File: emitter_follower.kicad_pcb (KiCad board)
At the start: 2 copper layers, 10 parts, among them Q2201 DNLS350E, Q2202 DPLS350E, Q2203 TIP41C, Q2204 TIP42C

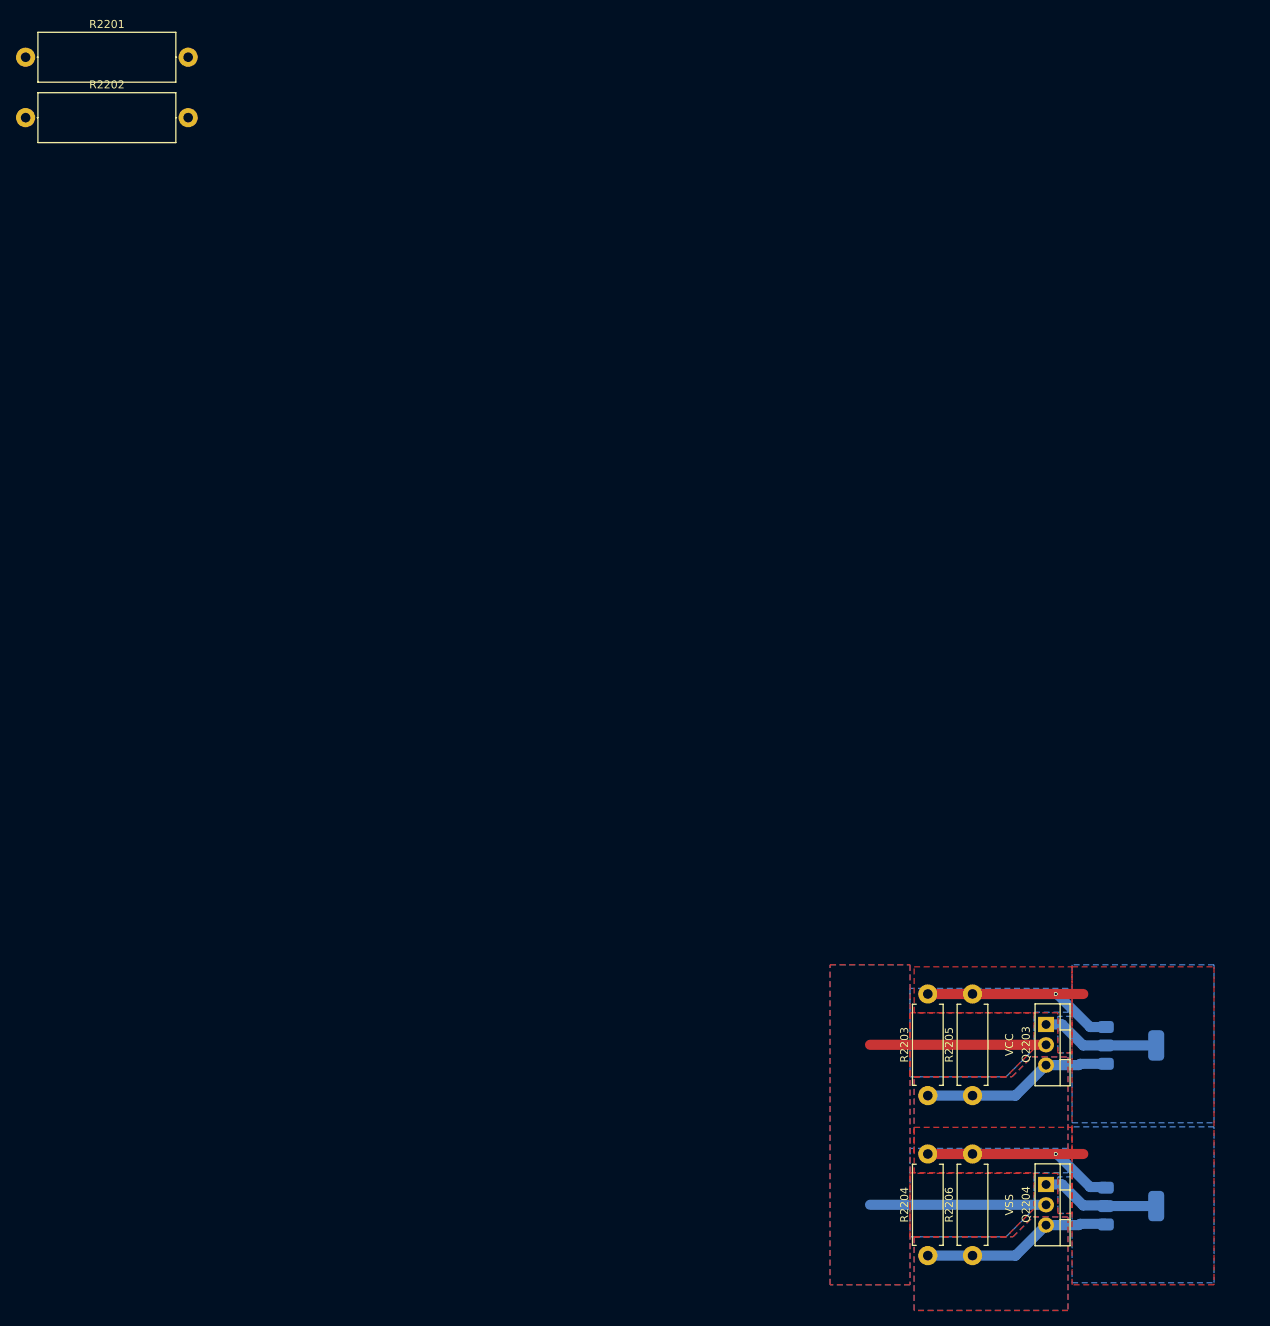
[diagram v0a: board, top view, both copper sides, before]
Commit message: add pcb outstage-unit sub circuit layout of power-electronics
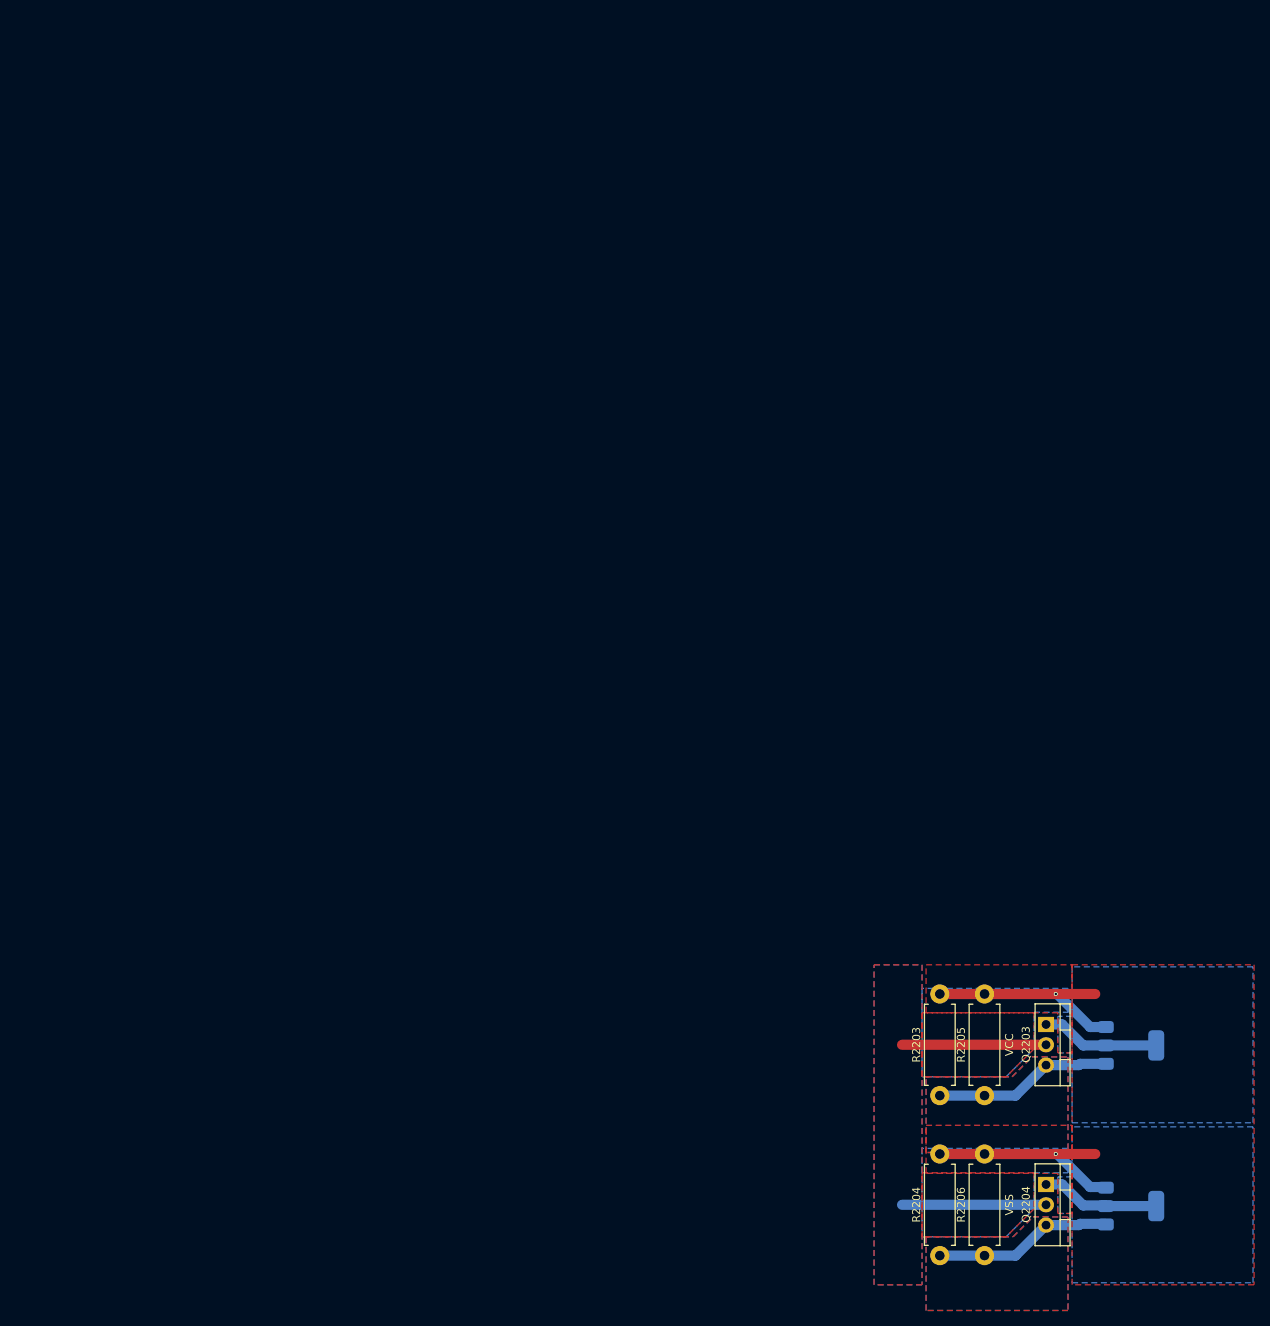
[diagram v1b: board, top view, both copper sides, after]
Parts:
- removed R2201, R2202: 22, pss:R_Axial_DIN0617_L17.0mm_D6.0mm_P20.32mm_Horizontal
- moved R2203 1.50 mm to (83.7, 116.3)
- moved R2204 1.50 mm to (83.7, 123.7)
- moved R2205 1.50 mm to (89.3, 116.3)
- moved R2206 1.50 mm to (89.3, 123.7)
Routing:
- net /VSS: track 22.0 -> 18.0 mm
- net /VCC: track 22.0 -> 18.0 mm
- net /v_out: track 86.8 -> 83.8 mm
- net /2: track 23.9 -> 22.4 mm
- net /1: track 23.9 -> 22.4 mm

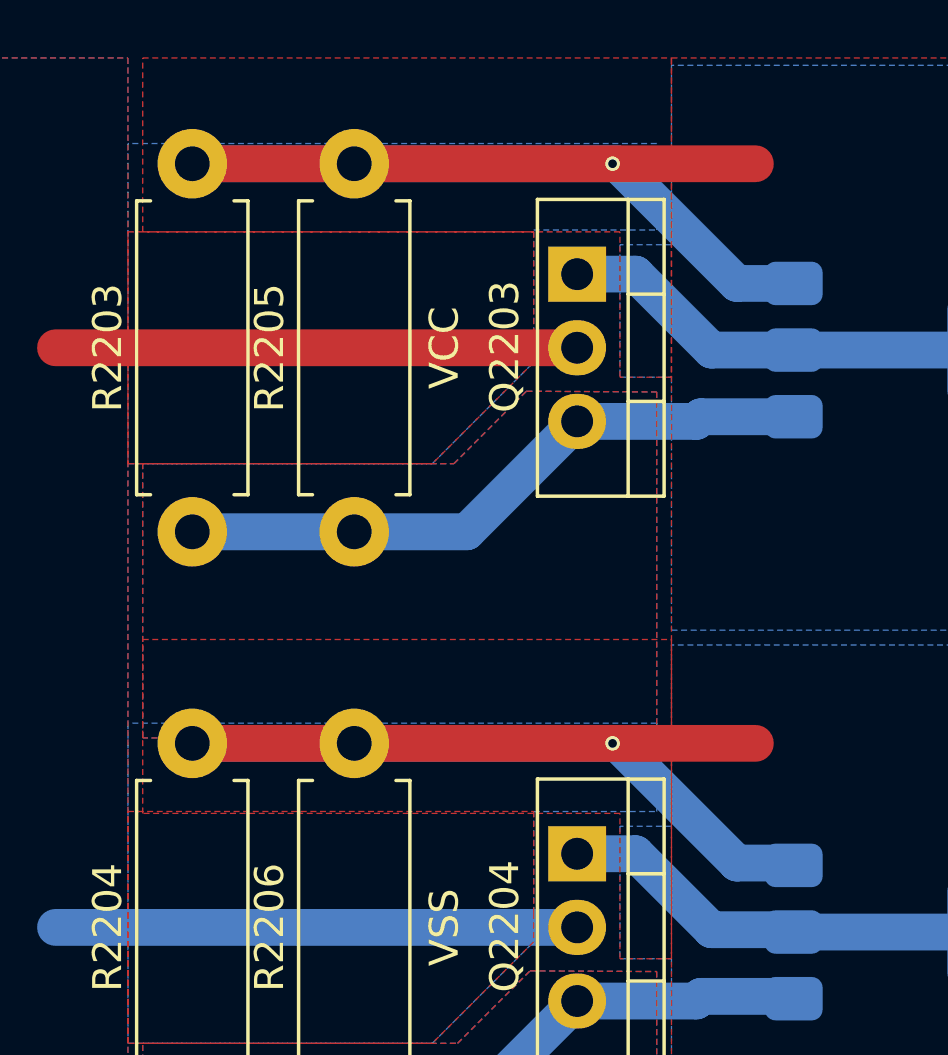
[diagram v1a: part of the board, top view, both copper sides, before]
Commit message: edit heatsink mounting holes position, fix copper pour
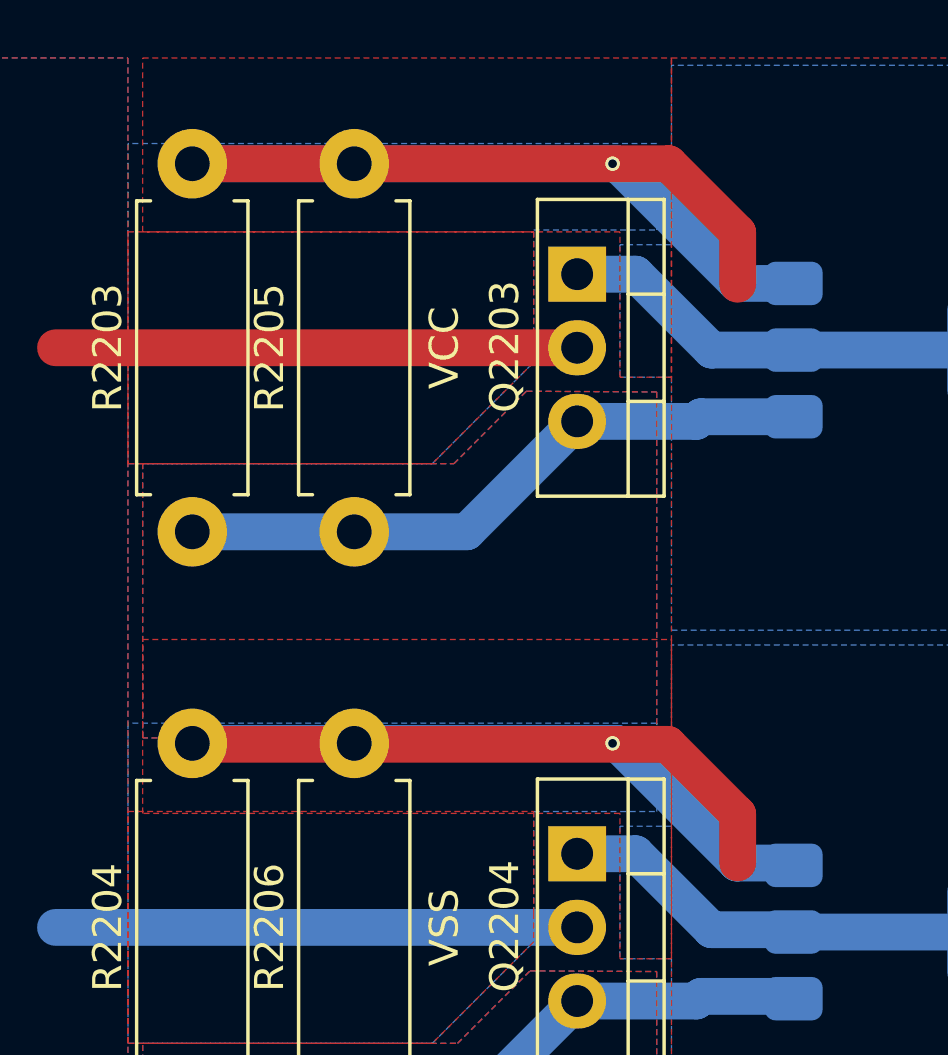
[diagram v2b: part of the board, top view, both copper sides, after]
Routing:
- net /v_out: track 83.8 -> 88.0 mm
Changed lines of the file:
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@@
+	)
+	(segment
+		(start 83.72 123.65)
+		(end 83.753 123.683)
+		(width 1.27)
+		(layer "F.Cu")
+		(net 1)
+	)
+	(segment
+		(start 102.54 106.03)
+		(end 102.54 107.808)
+		(width 1.27)
+		(layer "F.Cu")
+		(net 1)
+	)
+	(segment
+		(start 100.16 103.65)
+		(end 102.54 106.03)
+		(width 1.27)
+		(layer "F.Cu")
+		(net 1)
+	)
+	(segment
+		(start 83.753 123.683)
+		(end 100.127 123.683)
+		(width 1.27)
+		(layer "F.Cu")
+		(net 1)
+	)
+	(segment
+		(start 102.54 126.096)
+		(end 102.54 127.775)
+		(width 1.27)
+		(layer "F.Cu")
+		(net 1)
 	)
 	(segment
 		(start 83.72 103.65)
-		(end 103.15 103.65)
-		(width 1.27)
-		(layer "F.Cu")
-		(net 1)
-	)
-	(segment
-		(start 83.72 123.65)
-		(end 103.15 123.65)
+		(end 100.16 103.65)
+		(width 1.27)
+		(layer "F.Cu")
+		(net 1)
+	)
+	(segment
+		(start 100.127 123.683)
+		(end 102.54 126.096)
 		(width 1.27)
 		(layer "F.Cu")
@@
 		(layer "F.Cu")
 		(hatch edge 0.5)
-		(priority 90)
+		(priority 110)
 		(connect_pads
 			(clearance 0.508)
@@
 			(pts
 				(xy 81.5 106) (xy 95.5 106) (xy 95.5 109.5) (xy 95.5 110.5) (xy 92 114) (xy 81.5 114)
+			)
+		)
+	)
+	(zone
+		(net 0)
+		(net_name "")
+		(layers "F&B.Cu")
+		(hatch edge 0.5)
+		(connect_pads
+			(clearance 0)
+		)
+		(min_thickness 0.254)
+		(filled_areas_thickness no)
+		(keepout
+			(tracks allowed)
+			(vias allowed)
+			(pads allowed)
+			(copperpour not_allowed)
+			(footprints allowed)
+		)
+		(fill
+			(thermal_gap 0.508)
+			(thermal_bridge_width 1.27)
+		)
+		(polygon
+			(pts
+				(xy 82 140) (xy 81.5 140) (xy 81.5 134) (xy 82.008 134) (xy 82.008 139.992)
 			)
 		)
@@
 	)
 	(zone
+		(net 0)
+		(net_name "")
+		(layers "F&B.Cu")
+		(hatch edge 0.5)
+		(connect_pads
+			(clearance 0)
+		)
+		(min_thickness 0.254)
+		(filled_areas_thickness no)
+		(keepout
+			(tracks allowed)
+			(vias allowed)
+			(pads allowed)
+			(copperpour not_allowed)
+			(footprints allowed)
+		)
+		(fill
+			(thermal_gap 0.508)
+			(thermal_bridge_width 1.27)
+		)
+		(polygon
+			(pts
+				(xy 82 124.5) (xy 81.5 124) (xy 81.508 114) (xy 82.016 114)
+			)
+		)
+	)
+	(zone
 		(net 7)
 		(net_name "/2")
@@
 			)
 		)
+	)
+	(zone
+		(net 0)
+		(net_name "")
+		(layers "F&B.Cu")
+		(hatch edge 0.5)
+		(connect_pads
+			(clearance 0)
+		)
+		(min_thickness 0.254)
+		(filled_areas_thickness no)
+		(keepout
+			(tracks allowed)
+			(vias allowed)
+			(pads allowed)
+			(copperpour not_allowed)
+			(footprints allowed)
+		)
+		(fill
+			(thermal_gap 0.508)
+			(thermal_bridge_width 1.27)
+		)
+		(polygon
+			(pts
+				(xy 82.008 104.5) (xy 81.508 104) (xy 81.5 103.25) (xy 82.016 102.75)
+			)
+		)
